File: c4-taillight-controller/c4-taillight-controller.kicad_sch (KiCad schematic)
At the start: 0 parts

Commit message: created libraries with XL7015
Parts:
- added C1: C_Polarized, symbol Device:C_Polarized
- added D1: D_Zener, symbol Device:D_Zener
- added D2: D, symbol Device:D
- added PS1: XL7015, XL7015:CONV_XL7015, symbol XL7015:XL7015
- added Q1: Q_PMOS_GDS, symbol Transistor_FET:Q_PMOS_GDS
- added R1: 100k, symbol Device:R
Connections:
- new net: D1.2 (A), Q1.1 (G), R1.1
- new net GND: C1.2, D2.2 (A), PS1.3 (GND), PS1.6 (GND), R1.2
- new net VBAT_P: C1.1, D1.1 (K), D2.1 (K), Q1.3 (S)
- new net ~12V: Q1.2 (D)

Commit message: 8/12/2026 changes
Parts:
- removed PS1: XL7015, XL7015:CONV_XL7015, symbol XL7015:XL7015
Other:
- added sheet Block G MCU (block_G_mcu.kicad_sch)
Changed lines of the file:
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@@
-	)
-	(symbol
-		(lib_id "XL7015:XL7015")
-		(at 167.64 55.88 0)
-		(unit 1)
-		(body_style 1)
-		(exclude_from_sim no)
-		(in_bom yes)
-		(on_board yes)
-		(in_pos_files yes)
-		(dnp no)
-		(fields_autoplaced yes)
-		(property "Reference" "PS1"
-			(at 167.64 43.18 0)
-			(show_name no)
-			(do_not_autoplace no)
-			(effects
-				(font
-					(size 1.27 1.27)
-				)
-			)
-		)
-		(property "Value" "XL7015"
-			(at 167.64 45.72 0)
-			(show_name no)
-			(do_not_autoplace no)
-			(effects
-				(font
-					(size 1.27 1.27)
-				)
-			)
-		)
-		(property "Footprint" "XL7015:CONV_XL7015"
-			(at 167.64 55.88 0)
-			(hide yes)
-			(show_name no)
-			(do_not_autoplace no)
-			(effects
-				(font
-					(size 1.27 1.27)
-				)
-				(justify bottom)
-			)
-		)
-		(property "Datasheet" ""
-			(at 167.64 55.88 0)
-			(hide yes)
-			(show_name no)
-			(do_not_autoplace no)
-			(effects
-				(font
-					(size 1.27 1.27)
-				)
-			)
-		)
-		(property "Description" "0.8A 150KHz 80V Buck DC to DC"
-			(at 167.64 55.88 0)
-			(hide yes)
-			(show_name no)
-			(do_not_autoplace no)
-			(effects
-				(font
-					(size 1.27 1.27)
-				)
-				(justify bottom)
-			)
-		)
-		(property "MF" "XLSEMI"
-			(at 167.64 55.88 0)
-			(hide yes)
-			(show_name no)
-			(do_not_autoplace no)
-			(effects
-				(font
-					(size 1.27 1.27)
-				)
-				(justify bottom)
-			)
-		)
-		(property "MAXIMUM_PACKAGE_HEIGHT" "2.4mm"
-			(at 167.64 55.88 0)
-			(hide yes)
-			(show_name no)
-			(do_not_autoplace no)
-			(effects
-				(font
-					(size 1.27 1.27)
-				)
-				(justify bottom)
-			)
-		)
-		(property "CREATOR" "DIZAR"
-			(at 167.64 55.88 0)
-			(hide yes)
-			(show_name no)
-			(do_not_autoplace no)
-			(effects
-				(font
-					(size 1.27 1.27)
-				)
-				(justify bottom)
-			)
-		)
-		(property "Price" "None"
-			(at 167.64 55.88 0)
-			(hide yes)
-			(show_name no)
-			(do_not_autoplace no)
-			(effects
-				(font
-					(size 1.27 1.27)
-				)
-				(justify bottom)
-			)
-		)
-		(property "Package" "Package"
-			(at 167.64 55.88 0)
-			(hide yes)
-			(show_name no)
-			(do_not_autoplace no)
-			(effects
-				(font
-					(size 1.27 1.27)
-				)
-				(justify bottom)
-			)
-		)
-		(property "Check_prices" "https://www.snapeda.com/parts/XL7015/XLSEMI/view-part/?ref=eda"
-			(at 167.64 55.88 0)
-			(hide yes)
-			(show_name no)
-			(do_not_autoplace no)
-			(effects
-				(font
-					(size 1.27 1.27)
-				)
-				(justify bottom)
-			)
-		)
-		(property "STANDARD" "Manufacturer Recommendations"
-			(at 167.64 55.88 0)
-			(hide yes)
-			(show_name no)
-			(do_not_autoplace no)
-			(effects
-				(font
-					(size 1.27 1.27)
-				)
-				(justify bottom)
-			)
-		)
-		(property "PARTREV" "1.8"
-			(at 167.64 55.88 0)
-			(hide yes)
-			(show_name no)
-			(do_not_autoplace no)
-			(effects
-				(font
-					(size 1.27 1.27)
-				)
-				(justify bottom)
-			)
-		)
-		(property "VERIFIER" ""
-			(at 167.64 55.88 0)
-			(hide yes)
-			(show_name no)
-			(do_not_autoplace no)
-			(effects
-				(font
-					(size 1.27 1.27)
-				)
-				(justify bottom)
-			)
-		)
-		(property "SnapEDA_Link" "https://www.snapeda.com/parts/XL7015/XLSEMI/view-part/?ref=snap"
-			(at 167.64 55.88 0)
-			(hide yes)
-			(show_name no)
-			(do_not_autoplace no)
-			(effects
-				(font
-					(size 1.27 1.27)
-				)
-				(justify bottom)
-			)
-		)
-		(property "MP" "XL7015"
-			(at 167.64 55.88 0)
-			(hide yes)
-			(show_name no)
-			(do_not_autoplace no)
-			(effects
-				(font
-					(size 1.27 1.27)
-				)
-				(justify bottom)
-			)
-		)
-		(property "Availability" "In Stock"
-			(at 167.64 55.88 0)
-			(hide yes)
-			(show_name no)
-			(do_not_autoplace no)
-			(effects
-				(font
-					(size 1.27 1.27)
-				)
-				(justify bottom)
-			)
-		)
-		(property "MANUFACTURER" "XLSEMI"
-			(at 167.64 55.88 0)
-			(hide yes)
-			(show_name no)
-			(do_not_autoplace no)
-			(effects
-				(font
-					(size 1.27 1.27)
-				)
-				(justify bottom)
-			)
-		)
-		(pin "2"
-		)
-		(pin "1"
-		)
-		(pin "6"
-		)
-		(pin "5"
-		)
-		(pin "4"
-		)
-		(pin "3"
-		)
-		(instances
-			(project "c4-taillight-controller"
-				(path "/9b51997e-fe1e-4539-bed6-79e55e8c7cc2"
-					(reference "PS1")
-					(unit 1)
-				)
-			)
-		)
 	)
 	(symbol
@@
 				)
 			)
+		)
+	)
+	(sheet
+		(at 138.43 66.04)
+		(size 13.97 20.32)
+		(exclude_from_sim no)
+		(in_bom yes)
+		(on_board yes)
+		(dnp no)
+		(fields_autoplaced yes)
+		(stroke
+			(width 0.1524)
+			(type solid)
+		)
+		(fill
+			(color 0 0 0 0)
+		)
+		(property "Sheetname" "Block G MCU"
+			(at 138.43 65.3284 0)
+			(show_name no)
+			(do_not_autoplace no)
+			(effects
+				(font
+					(size 1.27 1.27)
+				)
+				(justify left bottom)
+			)
+		)
+		(property "Sheetfile" "block_G_mcu.kicad_sch"
+			(at 138.43 86.9446 0)
+			(show_name no)
+			(do_not_autoplace no)
+			(effects
+				(font
+					(size 1.27 1.27)
+				)
+				(justify left top)
+			)
+		)
+		(instances
+			(project "c4-taillight-controller"
+				(path "/9b51997e-fe1e-4539-bed6-79e55e8c7cc2"
+					(page "2")
+				)
+			)

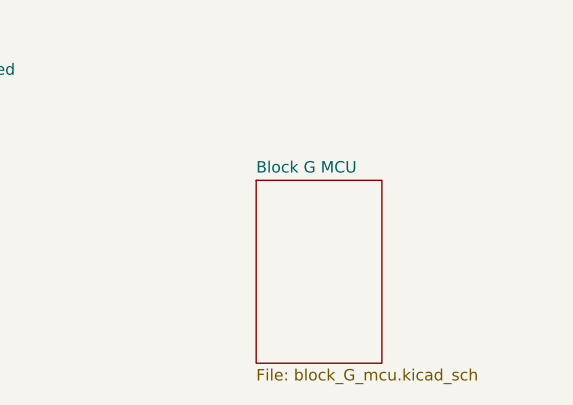
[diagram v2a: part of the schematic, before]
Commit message: 8/13/2026 changes. using nRF52840 instead of RP2040
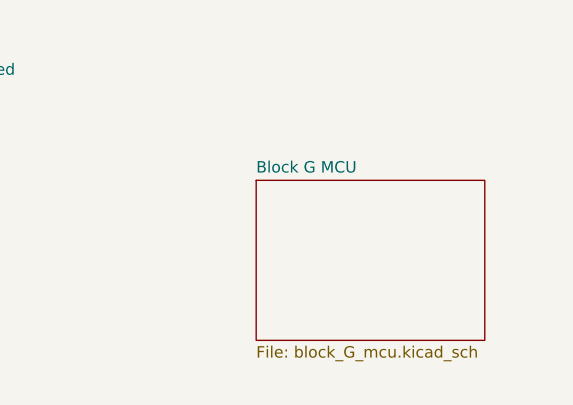
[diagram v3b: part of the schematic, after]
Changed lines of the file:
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@@
 	(sheet
 		(at 138.43 66.04)
-		(size 13.97 20.32)
+		(size 25.4 17.78)
 		(exclude_from_sim no)
 		(in_bom yes)
@@
 		)
 		(property "Sheetfile" "block_G_mcu.kicad_sch"
-			(at 138.43 86.9446 0)
+			(at 138.43 84.4046 0)
 			(show_name no)
 			(do_not_autoplace no)

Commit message: 8/14/2026 began MCU layout schematic
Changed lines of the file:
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@@
 	)
 	(sheet
-		(at 138.43 66.04)
+		(at 166.37 73.66)
 		(size 25.4 17.78)
 		(exclude_from_sim no)
@@
 		)
 		(property "Sheetname" "Block G MCU"
-			(at 138.43 65.3284 0)
+			(at 166.37 72.9484 0)
 			(show_name no)
 			(do_not_autoplace no)
@@
 		)
 		(property "Sheetfile" "block_G_mcu.kicad_sch"
-			(at 138.43 84.4046 0)
+			(at 166.37 92.0246 0)
 			(show_name no)
 			(do_not_autoplace no)

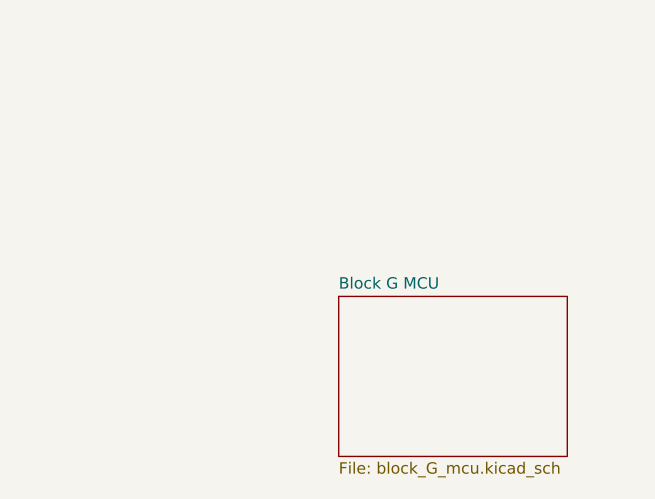
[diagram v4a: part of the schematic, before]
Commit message: Added new nRF52840 module board. MDBT50Q - U1MV2
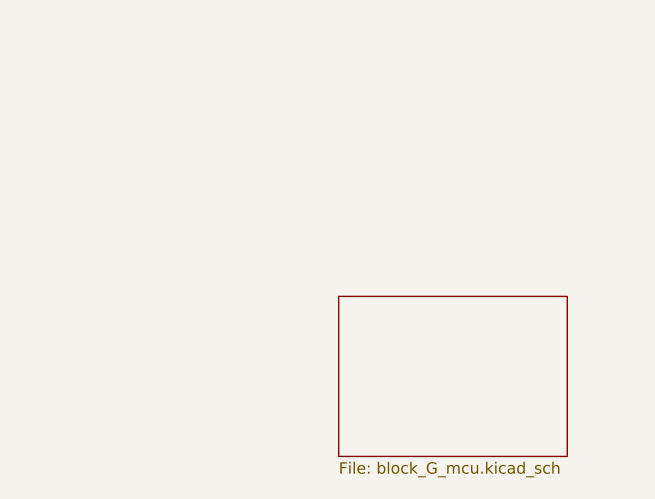
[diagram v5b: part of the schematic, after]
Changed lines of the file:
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@@
 		(property "Sheetname" "Block G MCU"
 			(at 166.37 72.9484 0)
+			(hide yes)
 			(show_name no)
 			(do_not_autoplace no)

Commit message: 8/17/2026 added MCU
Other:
- added sheet MCU (mcu.kicad_sch)
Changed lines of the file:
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@@
+		)
+	)
+	(sheet
+		(at 104.14 82.55)
+		(size 12.7 3.81)
+		(exclude_from_sim no)
+		(in_bom yes)
+		(on_board yes)
+		(dnp no)
+		(fields_autoplaced yes)
+		(stroke
+			(width 0.1524)
+			(type solid)
+		)
+		(fill
+			(color 0 0 0 0)
+		)
+		(property "Sheetname" "MCU"
+			(at 104.14 81.8384 0)
+			(show_name no)
+			(do_not_autoplace no)
+			(effects
+				(font
+					(size 1.27 1.27)
+				)
+				(justify left bottom)
+			)
+		)
+		(property "Sheetfile" "mcu.kicad_sch"
+			(at 104.14 86.9446 0)
+			(show_name no)
+			(do_not_autoplace no)
+			(effects
+				(font
+					(size 1.27 1.27)
+				)
+				(justify left top)
+			)
+		)
+		(instances
+			(project "c4-taillight-controller"
+				(path "/9b51997e-fe1e-4539-bed6-79e55e8c7cc2"
+					(page "3")
+				)
+			)
 		)
 	)

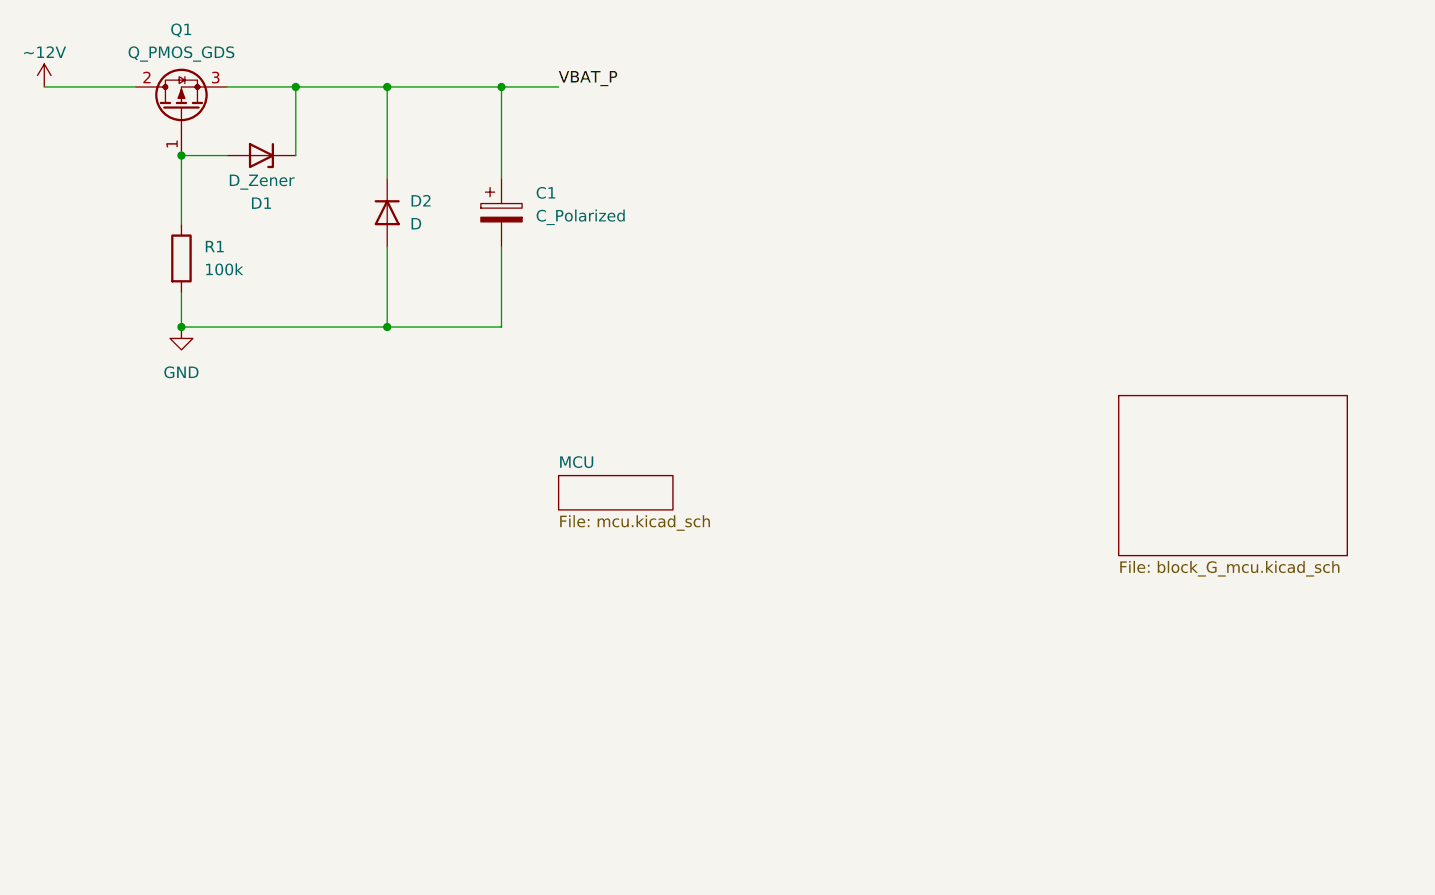
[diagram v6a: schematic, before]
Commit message: Finished complete layout of sheets
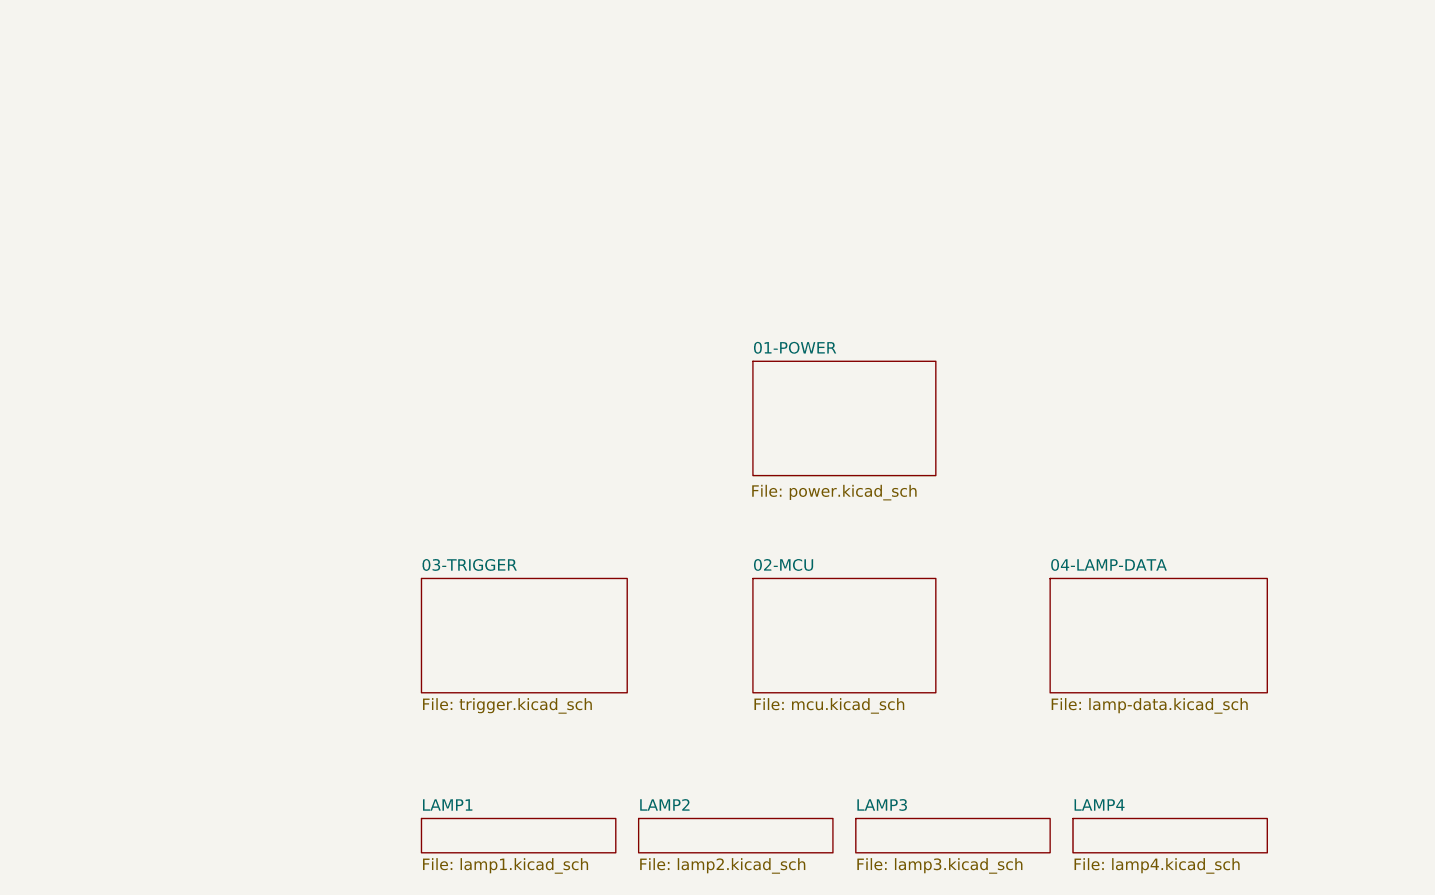
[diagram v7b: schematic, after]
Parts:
- removed C1: C_Polarized, symbol Device:C_Polarized
- removed D1: D_Zener, symbol Device:D_Zener
- removed D2: D, symbol Device:D
- removed Q1: Q_PMOS_GDS, symbol Transistor_FET:Q_PMOS_GDS
- removed R1: 100k, symbol Device:R
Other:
- sheet MCU renamed 02-MCU
- removed sheet Block G MCU
- added sheet 01-POWER (power.kicad_sch)
- added sheet 03-TRIGGER (trigger.kicad_sch)
- added sheet 04-LAMP-DATA (lamp-data.kicad_sch)
- added sheet LAMP1 (lamp1.kicad_sch)
- added sheet LAMP2 (lamp2.kicad_sch)
- added sheet LAMP3 (lamp3.kicad_sch)
- added sheet LAMP4 (lamp4.kicad_sch)
